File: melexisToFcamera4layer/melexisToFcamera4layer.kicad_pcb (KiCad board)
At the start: 4 copper layers, 56.6 x 57.7 mm, 104 parts, among them J1 Conn_01x01, J10 Conn_01x04, J11 Conn_01x04, J2 Conn_01x01, J3 Conn_01x01, J4 Conn_01x02, J5 Conn_01x01, J6 Conn_01x02, J7 Conn_01x01, J8 Conn_01x01, J9 Conn_01x04, U1 LM27762, U2 ADP2164, U3 MLX75023, U4 MIC23050_SYML, U5 Cmod_A7, U6 MIC23050_GYML, U7 MIC23050_GYML, U8 MLX75123

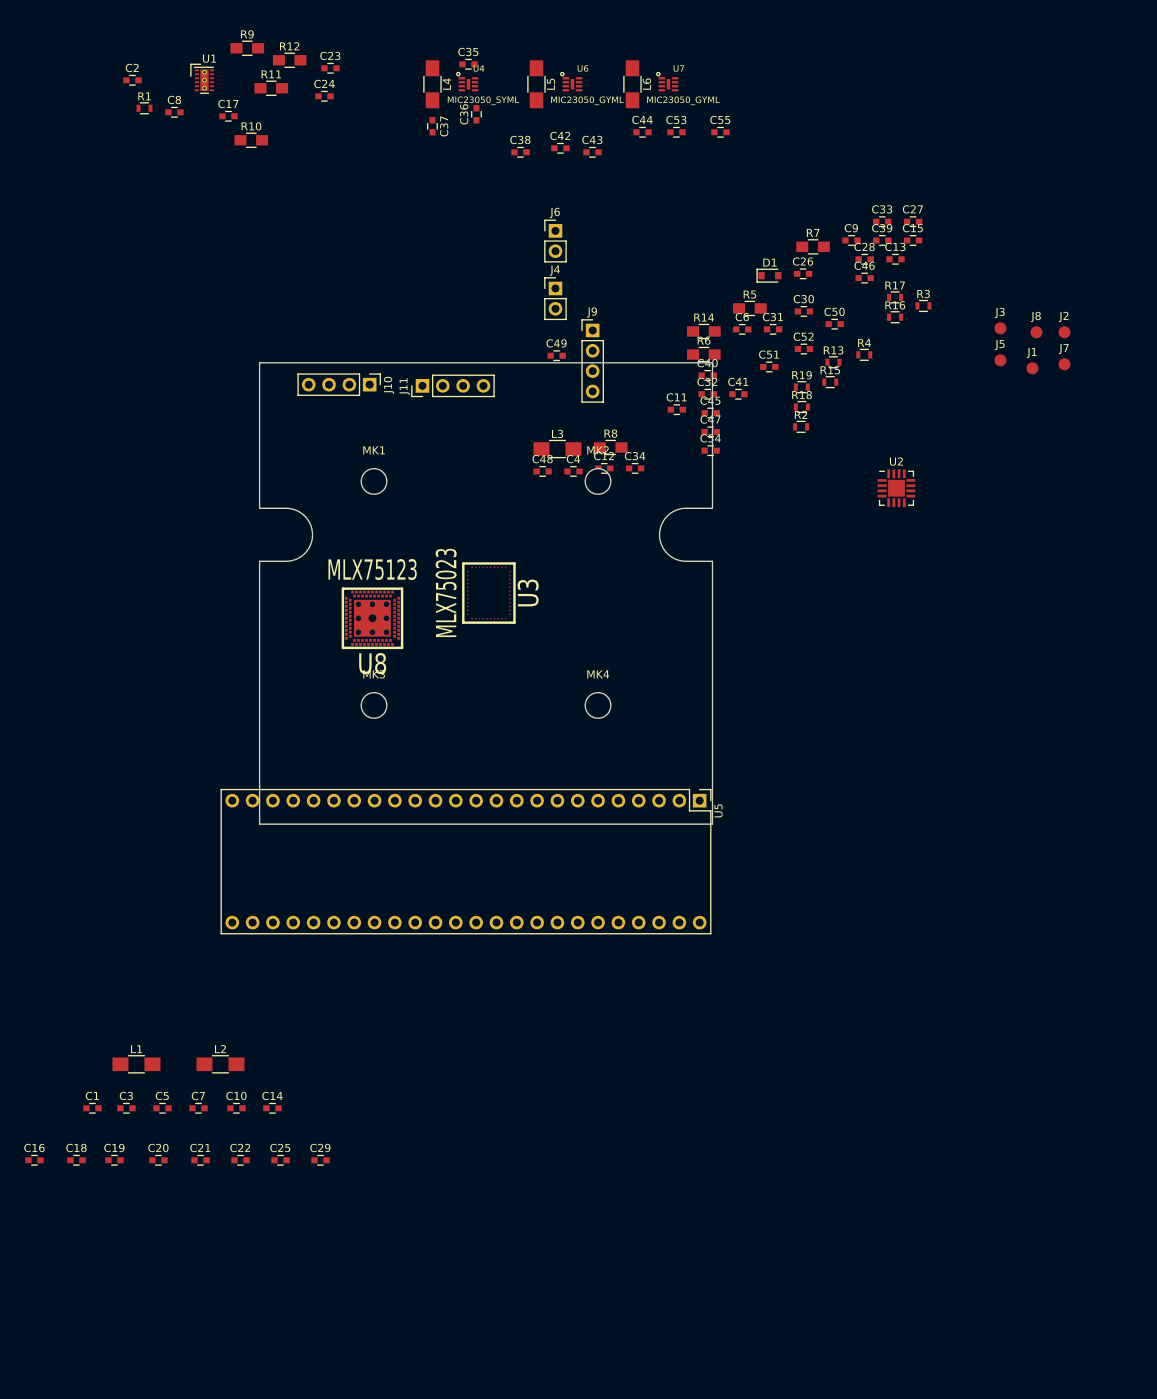
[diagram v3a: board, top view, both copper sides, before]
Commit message: Components on sensor board placed together
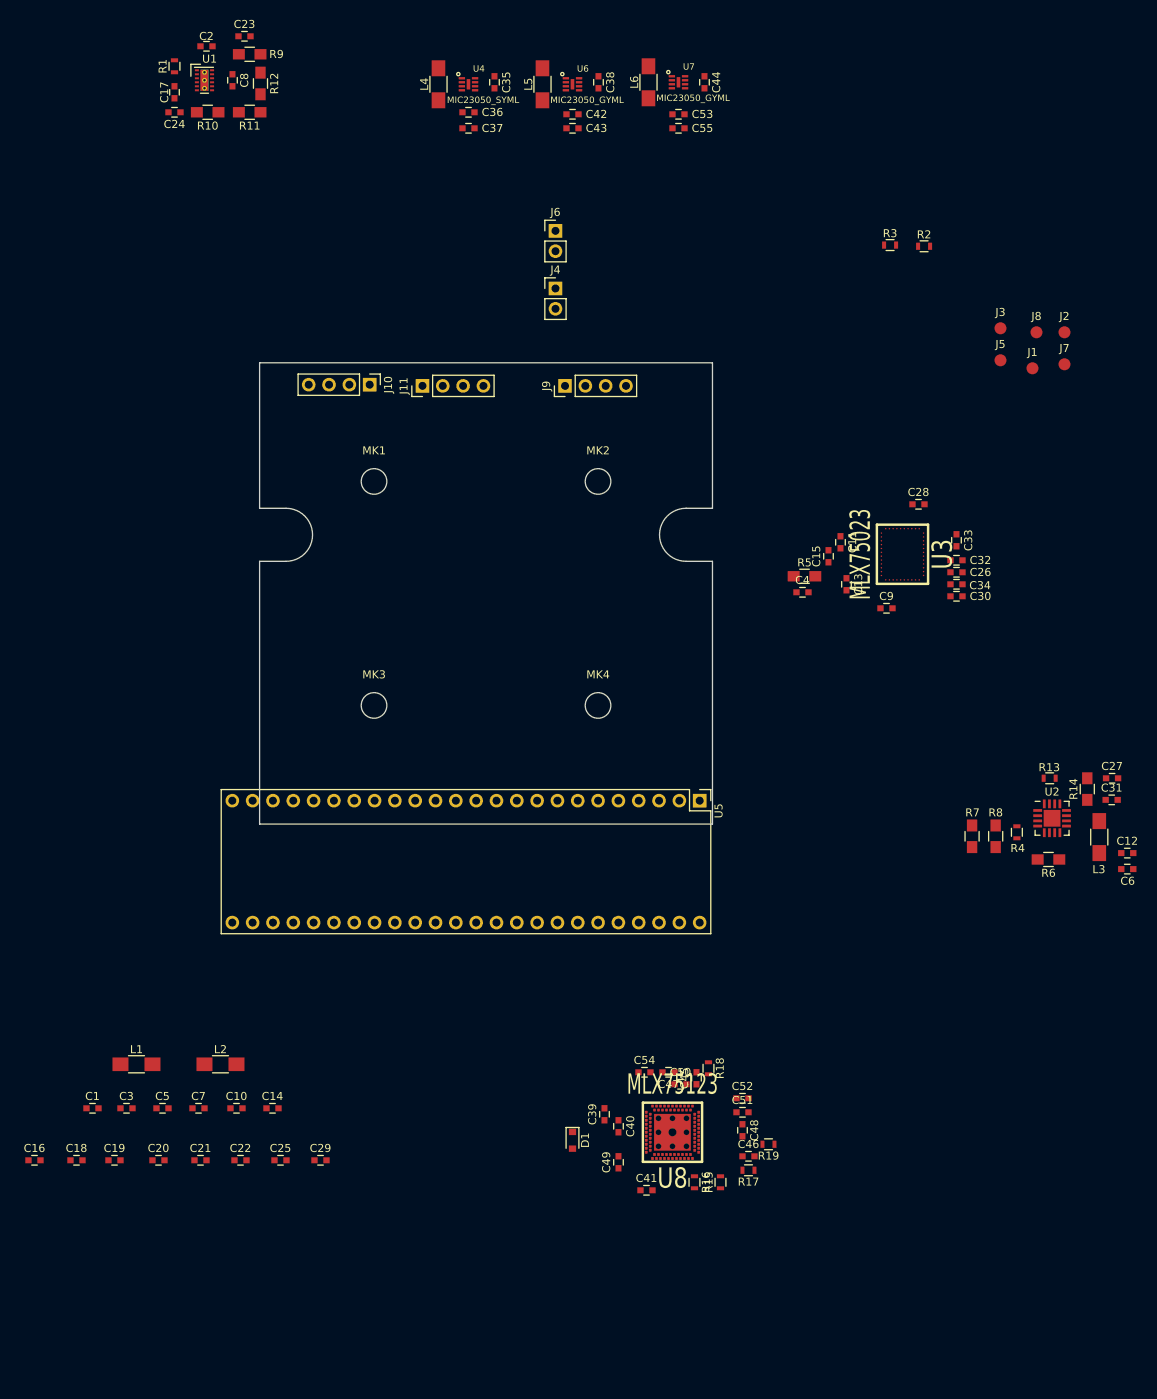
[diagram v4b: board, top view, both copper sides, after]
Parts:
- moved C39 114.6 mm to (116.5, 175.8), turned to 90 degrees
- moved R16 111.0 mm to (127.8, 184.2), turned to 270 degrees
- moved D1 110.9 mm to (112.5, 179.0), turned to 270 degrees
- moved C46 110.7 mm to (134.5, 181.0)
- moved R17 110.6 mm to (134.5, 182.8), turned to 180 degrees
- moved C49 101.1 mm to (118.2, 181.8), turned to 90 degrees
- moved R15 101.0 mm to (131.0, 184.2), turned to 90 degrees
- moved C41 100.2 mm to (121.8, 185.2)
- moved C50 97.0 mm to (126.0, 172.0)
- moved R19 94.7 mm to (137.0, 179.5), turned to 180 degrees
- moved C40 94.5 mm to (118.2, 177.2), turned to 270 degrees
- moved C52 94.0 mm to (133.8, 173.8)
- moved C51 93.2 mm to (133.8, 175.5)
- moved C48 86.1 mm to (133.8, 177.8), turned to 270 degrees
- moved R18 83.5 mm to (129.5, 170.0), turned to 270 degrees
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
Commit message: Improved schematics, prepared layout for routing
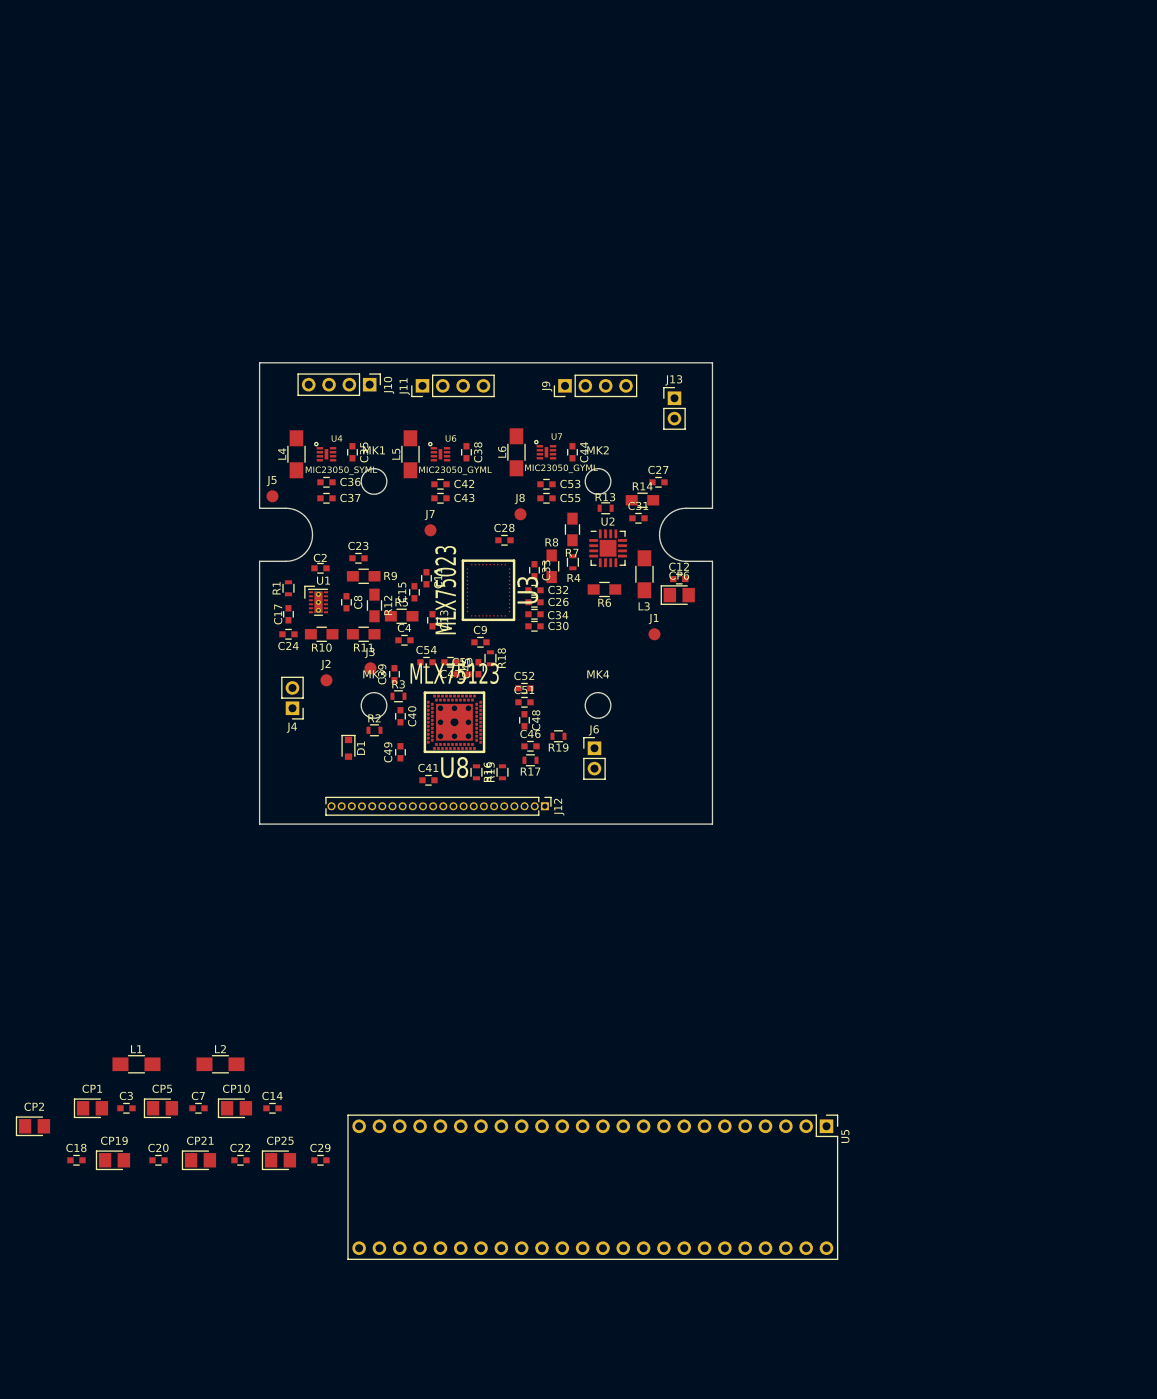
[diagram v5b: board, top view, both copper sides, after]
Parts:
- removed C1, C10, C16, C19, C21, C25, C5: 4u7, Capacitors_SMD:C_0603
- removed C6: 150u, Capacitors_SMD:C_0603
- added CP1: 4u7, Capacitors_Tantalum_SMD:CP_Tantalum_Case-R_EIA-2012-12_Reflow, F.Cu at (52.5, 175.0)
- added CP10: 4u7, Capacitors_Tantalum_SMD:CP_Tantalum_Case-R_EIA-2012-12_Reflow, F.Cu at (70.5, 175.0)
- added CP19: 4u7, Capacitors_Tantalum_SMD:CP_Tantalum_Case-R_EIA-2012-12_Reflow, F.Cu at (55.2, 181.5)
- added CP2: 4u7, Capacitors_Tantalum_SMD:CP_Tantalum_Case-R_EIA-2012-12_Reflow, F.Cu at (45.2, 177.2)
- added CP21: 4u7, Capacitors_Tantalum_SMD:CP_Tantalum_Case-R_EIA-2012-12_Reflow, F.Cu at (66.0, 181.5)
- added CP25: 4u7, Capacitors_Tantalum_SMD:CP_Tantalum_Case-R_EIA-2012-12_Reflow, F.Cu at (76.0, 181.5)
- added CP5: 4u7, Capacitors_Tantalum_SMD:CP_Tantalum_Case-R_EIA-2012-12_Reflow, F.Cu at (61.2, 175.0)
- added CP6: 150u, Capacitors_Tantalum_SMD:CP_Tantalum_Case-R_EIA-2012-12_Reflow, F.Cu at (125.8, 110.8)
- added J12: Conn_01x22, Pin_Headers:Pin_Header_Straight_1x22_Pitch1.27mm, F.Cu at (109.0, 137.2)
- added J13: Conn_01x02, Pin_Headers:Pin_Header_Straight_1x02_Pitch2.54mm, F.Cu at (125.2, 86.2)
- moved J2 102.0 mm to (81.8, 121.5)
- moved J5 92.6 mm to (75.0, 98.5)
- moved R2 91.5 mm to (87.8, 127.8)
- moved J3 89.5 mm to (87.2, 120.0)
- moved R3 83.4 mm to (90.8, 123.5)
- moved J7 81.9 mm to (94.8, 102.8)
- moved C31 68.8 mm to (120.8, 101.2)
- moved J8 68.4 mm to (106.0, 100.8)
- moved C27 67.7 mm to (123.2, 96.8)
- moved C17 66.8 mm to (77.0, 113.2)
- moved C2 66.8 mm to (81.0, 107.5)
- moved C23 66.8 mm to (85.8, 106.2)
- moved C24 66.8 mm to (77.0, 115.8)
- moved C8 66.8 mm to (84.2, 111.8)
- moved R1 66.8 mm to (77.0, 110.0)
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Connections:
- C42 pad 1: /VDD3V3 -> /VDD1V8
- C43 pad 1: /VDD3V3 -> /VDD1V8
- C53 pad 1: /VDD3V3 -> /VDD1V8_clean
- C55 pad 1: /VDD3V3 -> /VDD1V8_clean
- J4 pad 1: Net-(J4-Pad1) -> +5V
- J7 pad 1: /VDD3V3 -> /VDD1V8
- J8 pad 1: /VDD3V3 -> /VDD1V8_clean
- L5 pad 2: /VDD3V3 -> /VDD1V8
- L6 pad 2: /VDD3V3 -> /VDD1V8_clean
- U5 pad 24: Net-(J4-Pad1) -> Net-(J13-Pad1)
- U6 pad 4: /VDD3V3 -> /VDD1V8
- U7 pad 4: /VDD3V3 -> /VDD1V8_clean
- U8 pad A33: (no net) -> GND
